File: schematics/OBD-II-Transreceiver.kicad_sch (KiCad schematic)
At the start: 5 parts, among them IC2 MCP2551T-E_SN, Q1 MOSFET, Q2 TRNSSTR

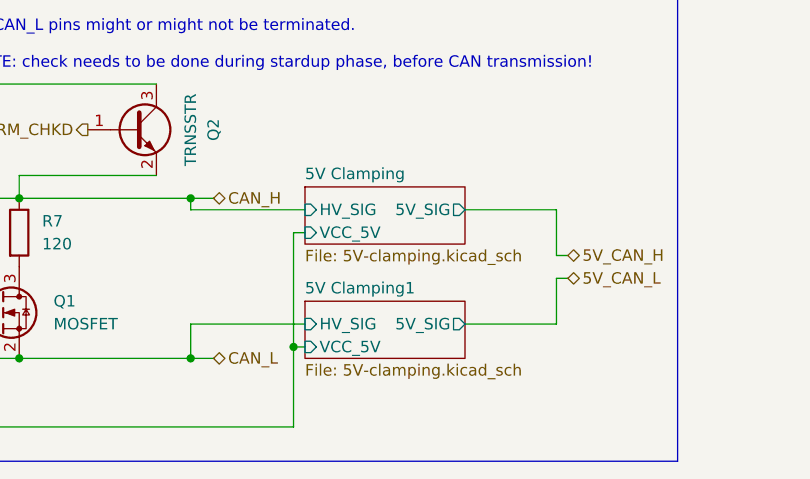
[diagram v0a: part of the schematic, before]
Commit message: OBD II clamping schematic simplification; README file update. Small repositionings.
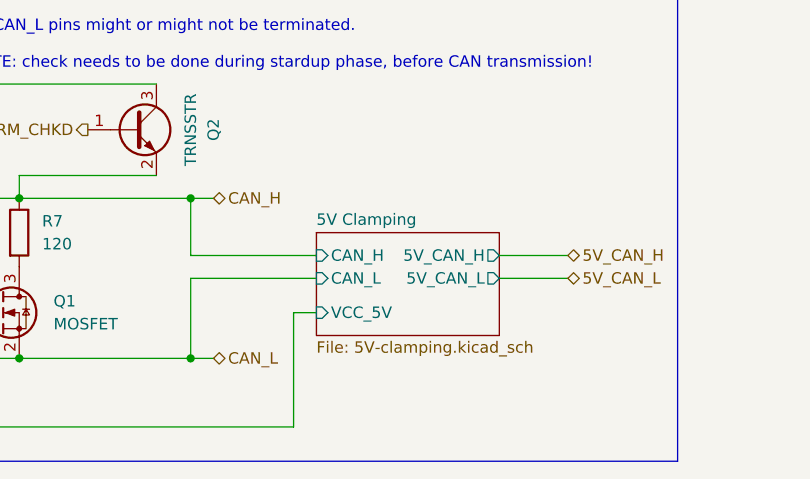
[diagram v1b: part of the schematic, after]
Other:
- removed sheet 5V Clamping1
- sheet 5V Clamping ports: added 5V_CAN_H, 5V_CAN_L, CAN_H, CAN_L; removed 5V_SIG, HV_SIG
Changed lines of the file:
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@@
+	)
+	(junction
+		(at 52.07 74.93)
+		(diameter 0)
+		(color 0 0 0 0)
 	)
 	(junction
@@
 	)
 	(junction
-		(at 148.59 73.66)
-		(diameter 0)
-		(color 0 0 0 0)
-	)
-	(junction
-		(at 52.07 74.93)
+		(at 118.11 74.93)
 		(diameter 0)
 		(color 0 0 0 0)
@@
 	)
 	(junction
-		(at 118.11 74.93)
-		(diameter 0)
-		(color 0 0 0 0)
-	)
-	(junction
 		(at 118.11 57.15)
 		(diameter 0)
@@
 	(wire
 		(pts
-			(xy 177.8 71.12) (xy 167.64 71.12)
+			(xy 137.16 63.5) (xy 151.13 63.5)
 		)
 		(stroke
@@
 	(wire
 		(pts
+			(xy 137.16 74.93) (xy 137.16 66.04)
+		)
+		(stroke
+			(width 0)
+			(type default)
+		)
+	)
+	(wire
+		(pts
+			(xy 148.59 69.85) (xy 151.13 69.85)
+		)
+		(stroke
+			(width 0)
+			(type default)
+		)
+	)
+	(wire
+		(pts
 			(xy 91.44 72.39) (xy 88.9 72.39)
 		)
@@
 	(wire
 		(pts
+			(xy 137.16 57.15) (xy 137.16 63.5)
+		)
+		(stroke
+			(width 0)
+			(type default)
+		)
+	)
+	(wire
+		(pts
 			(xy 91.44 57.15) (xy 91.44 72.39)
 		)
@@
 	(wire
 		(pts
-			(xy 137.16 74.93) (xy 137.16 71.12)
-		)
-		(stroke
-			(width 0)
-			(type default)
-		)
-	)
-	(wire
-		(pts
-			(xy 148.59 73.66) (xy 148.59 60.96)
-		)
-		(stroke
-			(width 0)
-			(type default)
-		)
-	)
-	(wire
-		(pts
 			(xy 118.11 57.15) (xy 137.16 57.15)
 		)
@@
 	(wire
 		(pts
-			(xy 137.16 58.42) (xy 149.86 58.42)
-		)
-		(stroke
-			(width 0)
-			(type default)
-		)
-	)
-	(wire
-		(pts
-			(xy 148.59 73.66) (xy 149.86 73.66)
-		)
-		(stroke
-			(width 0)
-			(type default)
-		)
-	)
-	(wire
-		(pts
-			(xy 137.16 57.15) (xy 137.16 58.42)
-		)
-		(stroke
-			(width 0)
-			(type default)
-		)
-	)
-	(wire
-		(pts
-			(xy 148.59 60.96) (xy 149.86 60.96)
+			(xy 52.07 54.61) (xy 52.07 74.93)
+		)
+		(stroke
+			(width 0)
+			(type default)
+		)
+	)
+	(wire
+		(pts
+			(xy 52.07 74.93) (xy 52.07 82.55)
+		)
+		(stroke
+			(width 0)
+			(type default)
+		)
+	)
+	(wire
+		(pts
+			(xy 118.11 74.93) (xy 137.16 74.93)
+		)
+		(stroke
+			(width 0)
+			(type default)
+		)
+	)
+	(wire
+		(pts
+			(xy 49.53 74.93) (xy 52.07 74.93)
+		)
+		(stroke
+			(width 0)
+			(type default)
+		)
+	)
+	(wire
+		(pts
+			(xy 133.35 54.61) (xy 118.11 54.61)
+		)
+		(stroke
+			(width 0)
+			(type default)
+		)
+	)
+	(wire
+		(pts
+			(xy 137.16 74.93) (xy 139.7 74.93)
+		)
+		(stroke
+			(width 0)
+			(type default)
+		)
+	)
+	(wire
+		(pts
+			(xy 101.6 54.61) (xy 52.07 54.61)
 		)
 		(stroke
@@
 	(wire
 		(pts
-			(xy 52.07 54.61) (xy 52.07 74.93)
-		)
-		(stroke
-			(width 0)
-			(type default)
-		)
-	)
-	(wire
-		(pts
-			(xy 177.8 63.5) (xy 179.07 63.5)
-		)
-		(stroke
-			(width 0)
-			(type default)
-		)
-	)
-	(wire
-		(pts
-			(xy 52.07 74.93) (xy 52.07 82.55)
-		)
-		(stroke
-			(width 0)
-			(type default)
-		)
-	)
-	(wire
-		(pts
-			(xy 177.8 66.04) (xy 177.8 71.12)
-		)
-		(stroke
-			(width 0)
-			(type default)
-		)
-	)
-	(wire
-		(pts
-			(xy 137.16 74.93) (xy 139.7 74.93)
-		)
-		(stroke
-			(width 0)
-			(type default)
-		)
-	)
-	(wire
-		(pts
-			(xy 49.53 74.93) (xy 52.07 74.93)
-		)
-		(stroke
-			(width 0)
-			(type default)
-		)
-	)
-	(wire
-		(pts
-			(xy 133.35 54.61) (xy 118.11 54.61)
-		)
-		(stroke
-			(width 0)
-			(type default)
-		)
-	)
-	(wire
-		(pts
-			(xy 101.6 54.61) (xy 52.07 54.61)
-		)
-		(stroke
-			(width 0)
-			(type default)
-		)
-	)
-	(wire
-		(pts
-			(xy 148.59 82.55) (xy 148.59 73.66)
+			(xy 171.45 63.5) (xy 179.07 63.5)
+		)
+		(stroke
+			(width 0)
+			(type default)
+		)
+	)
+	(wire
+		(pts
+			(xy 171.45 66.04) (xy 179.07 66.04)
 		)
 		(stroke
@@
 	(wire
 		(pts
-			(xy 137.16 71.12) (xy 149.86 71.12)
-		)
-		(stroke
-			(width 0)
-			(type default)
-		)
-	)
-	(wire
-		(pts
-			(xy 118.11 74.93) (xy 137.16 74.93)
-		)
-		(stroke
-			(width 0)
-			(type default)
-		)
-	)
-	(wire
-		(pts
-			(xy 177.8 66.04) (xy 179.07 66.04)
-		)
-		(stroke
-			(width 0)
-			(type default)
-		)
-	)
-	(wire
-		(pts
-			(xy 177.8 58.42) (xy 177.8 63.5)
+			(xy 148.59 82.55) (xy 148.59 69.85)
 		)
 		(stroke
@@
 	(wire
 		(pts
-			(xy 177.8 58.42) (xy 167.64 58.42)
+			(xy 137.16 66.04) (xy 151.13 66.04)
 		)
 		(stroke
@@
 	)
 	(sheet
-		(at 149.86 55.88)
-		(size 17.78 6.35)
+		(at 151.13 60.96)
+		(size 20.32 11.43)
 		(exclude_from_sim no)
 		(in_bom yes)
@@
 		)
 		(property "Sheetname" "5V Clamping"
-			(at 149.86 55.1684 0)
+			(at 151.13 60.2484 0)
 			(effects
 				(font
@@
 		)
 		(property "Sheetfile" "5V-clamping.kicad_sch"
-			(at 149.86 62.8146 0)
+			(at 151.13 72.9746 0)
 			(effects
 				(font
@@
 			)
 		)
-		(pin "5V_SIG" output
-			(at 167.64 58.42 0)
+		(pin "VCC_5V" input
+			(at 151.13 69.85 180)
+			(effects
+				(font
+					(size 1.27 1.27)
+				)
+				(justify left)
+			)
+		)
+		(pin "5V_CAN_H" output
+			(at 171.45 63.5 0)
 			(effects
 				(font
@@
 			)
 		)
-		(pin "HV_SIG" input
-			(at 149.86 58.42 180)
-			(effects
-				(font
-					(size 1.27 1.27)
-				)
-				(justify left)
-			)
-		)
-		(pin "VCC_5V" input
-			(at 149.86 60.96 180)
+		(pin "5V_CAN_L" output
+			(at 171.45 66.04 0)
+			(effects
+				(font
+					(size 1.27 1.27)
+				)
+				(justify right)
+			)
+		)
+		(pin "CAN_H" input
+			(at 151.13 63.5 180)
+			(effects
+				(font
+					(size 1.27 1.27)
+				)
+				(justify left)
+			)
+		)
+		(pin "CAN_L" input
+			(at 151.13 66.04 180)
 			(effects
 				(font
@@
 				)
 			)
-		)
-	)
-	(sheet
-		(at 149.86 68.58)
-		(size 17.78 6.35)
-		(exclude_from_sim no)
-		(in_bom yes)
-		(on_board yes)
-		(dnp no)
-		(fields_autoplaced yes)
-		(stroke
-			(width 0.1524)
-			(type solid)
-		)
-		(fill
-			(color 0 0 0 0.0000)
-		)
-		(property "Sheetname" "5V Clamping1"
-			(at 149.86 67.8684 0)
-			(effects
-				(font
-					(size 1.27 1.27)
-				)
-				(justify left bottom)
-			)
-		)
-		(property "Sheetfile" "5V-clamping.kicad_sch"
-			(at 149.86 75.5146 0)
-			(effects
-				(font
-					(size 1.27 1.27)
-				)
-				(justify left top)
-			)
-		)
-		(pin "5V_SIG" output
-			(at 167.64 71.12 0)
-			(effects
-				(font
-					(size 1.27 1.27)
-				)
-				(justify right)
-			)
-		)
-		(pin "HV_SIG" input
-			(at 149.86 71.12 180)
-			(effects
-				(font
-					(size 1.27 1.27)
-				)
-				(justify left)
-			)
-		)
-		(pin "VCC_5V" input
-			(at 149.86 73.66 180)
-			(effects
-				(font
-					(size 1.27 1.27)
-				)
-				(justify left)
-			)
-		)
-		(instances
-			(project "bike-sensors-logger"
-				(path "/2c1d9222-af16-428b-85a5-a3d420373d70/23f3389a-4f90-491e-9f31-2a46e142f2be"
-					(page "3")
-				)
-			)

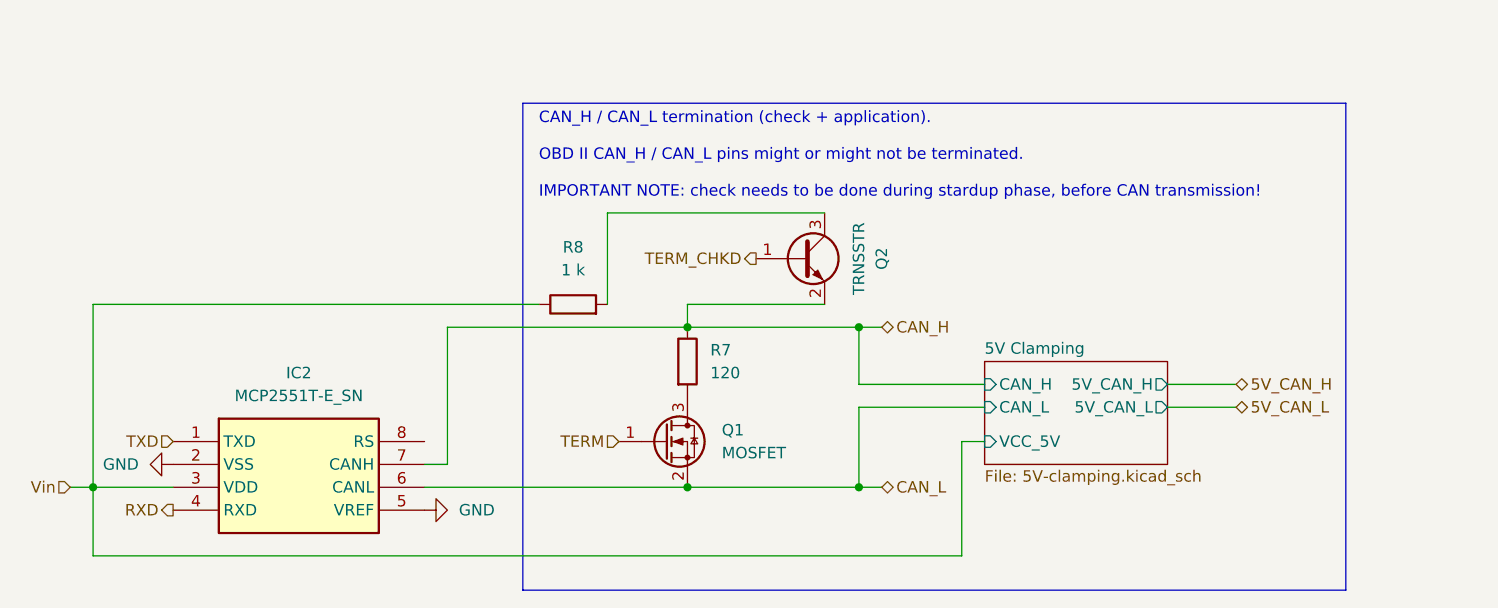
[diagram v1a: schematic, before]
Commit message: Fixed OBD II termination check (schem + firm)
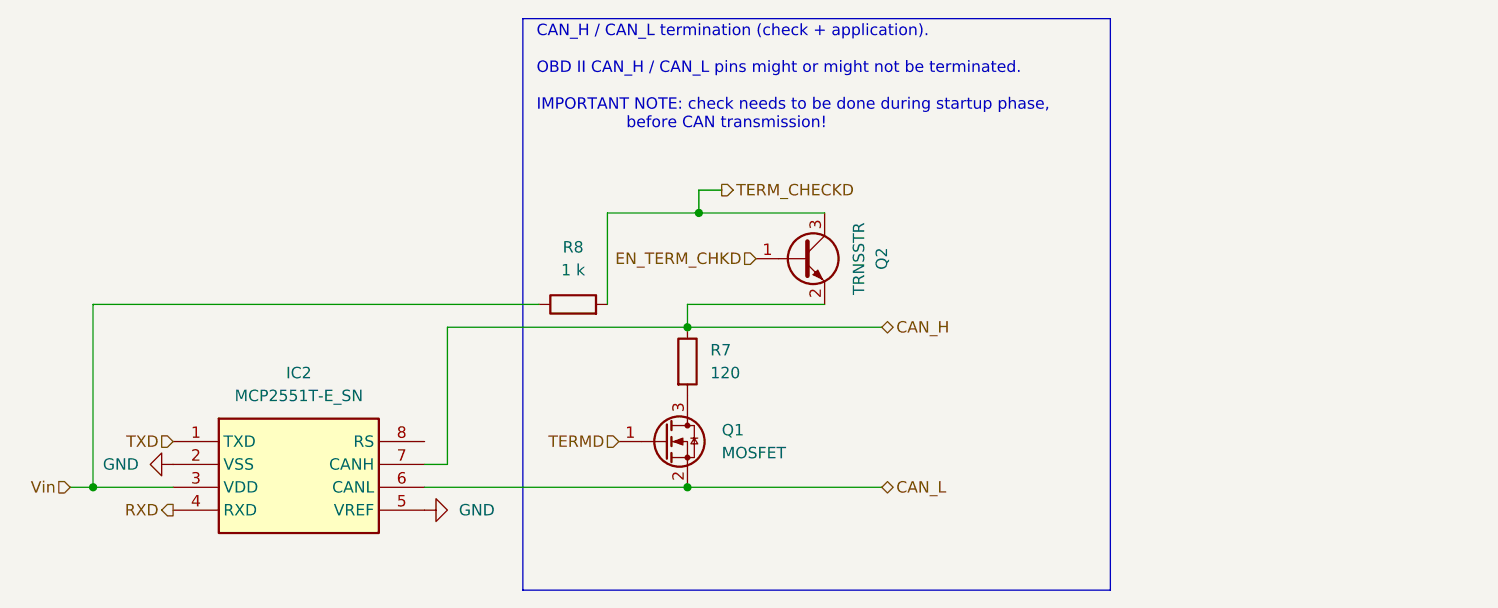
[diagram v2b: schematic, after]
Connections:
- net TERM_CHECKD: now reaches Q2.3 (C), R8.2
- net TERM renamed TERMD
- net TERM_CHKD renamed EN_TERM_CHKD
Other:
- removed sheet 5V Clamping
- note added: "CAN_H / CAN_L termination (check + application). OBD II CAN_H / CAN_L pins might or might not be terminated. IMPORTANT NOTE: check needs to be done during startup phase, before CAN transmission!"
- note removed: "CAN_H / CAN_L termination (check + application). OBD II CAN_H / CAN_L pins might or might not be terminated. IMPORTANT NOTE: check needs to be done during stardup phase, before CAN transmission!"
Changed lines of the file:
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@@
 	)
 	(rectangle
-		(start 99.822 32.258)
-		(end 191.262 86.36)
+		(start 99.822 22.86)
+		(end 165.1 86.36)
 		(stroke
 			(width 0)
@@
 		)
 	)
-	(text "CAN_H / CAN_L termination (check + application).\n\nOBD II CAN_H / CAN_L pins might or might not be terminated.\n\nIMPORTANT NOTE: check needs to be done during stardup phase, before CAN transmission!"
+	(text "CAN_H / CAN_L termination (check + application).\n\nOBD II CAN_H / CAN_L pins might or might not be terminated.\n\nIMPORTANT NOTE: check needs to be done during startup phase,\n                  before CAN transmission!"
 		(exclude_from_sim no)
-		(at 101.6 38.1 0)
+		(at 101.346 29.464 0)
 		(effects
 			(font
@@
 			(justify left)
 		)
+	)
+	(junction
+		(at 119.38 44.45)
+		(diameter 0)
+		(color 0 0 0 0)
 	)
 	(junction
@@
 	)
 	(junction
-		(at 137.16 74.93)
-		(diameter 0)
-		(color 0 0 0 0)
-	)
-	(junction
 		(at 118.11 74.93)
-		(diameter 0)
-		(color 0 0 0 0)
-	)
-	(junction
-		(at 137.16 57.15)
 		(diameter 0)
 		(color 0 0 0 0)
@@
 	(wire
 		(pts
-			(xy 137.16 63.5) (xy 151.13 63.5)
-		)
-		(stroke
-			(width 0)
-			(type default)
-		)
-	)
-	(wire
-		(pts
 			(xy 109.22 54.61) (xy 109.22 44.45)
 		)
@@
 	(wire
 		(pts
-			(xy 137.16 74.93) (xy 137.16 66.04)
-		)
-		(stroke
-			(width 0)
-			(type default)
-		)
-	)
-	(wire
-		(pts
-			(xy 148.59 69.85) (xy 151.13 69.85)
-		)
-		(stroke
-			(width 0)
-			(type default)
-		)
-	)
-	(wire
-		(pts
 			(xy 91.44 72.39) (xy 88.9 72.39)
 		)
@@
 	(wire
 		(pts
-			(xy 109.22 44.45) (xy 133.35 44.45)
-		)
-		(stroke
-			(width 0)
-			(type default)
-		)
-	)
-	(wire
-		(pts
 			(xy 91.44 57.15) (xy 118.11 57.15)
 		)
@@
 	(wire
 		(pts
-			(xy 137.16 57.15) (xy 137.16 63.5)
-		)
-		(stroke
-			(width 0)
-			(type default)
-		)
-	)
-	(wire
-		(pts
 			(xy 91.44 57.15) (xy 91.44 72.39)
 		)
@@
 	(wire
 		(pts
-			(xy 118.11 57.15) (xy 137.16 57.15)
+			(xy 118.11 57.15) (xy 139.7 57.15)
 		)
 		(stroke
@@
 	(wire
 		(pts
-			(xy 52.07 74.93) (xy 52.07 82.55)
-		)
-		(stroke
-			(width 0)
-			(type default)
-		)
-	)
-	(wire
-		(pts
-			(xy 118.11 74.93) (xy 137.16 74.93)
+			(xy 119.38 41.91) (xy 119.38 44.45)
+		)
+		(stroke
+			(width 0)
+			(type default)
+		)
+	)
+	(wire
+		(pts
+			(xy 109.22 44.45) (xy 119.38 44.45)
+		)
+		(stroke
+			(width 0)
+			(type default)
+		)
+	)
+	(wire
+		(pts
+			(xy 119.38 44.45) (xy 133.35 44.45)
+		)
+		(stroke
+			(width 0)
+			(type default)
+		)
+	)
+	(wire
+		(pts
+			(xy 118.11 74.93) (xy 139.7 74.93)
 		)
 		(stroke
@@
 	(wire
 		(pts
-			(xy 137.16 74.93) (xy 139.7 74.93)
-		)
-		(stroke
-			(width 0)
-			(type default)
-		)
-	)
-	(wire
-		(pts
 			(xy 101.6 54.61) (xy 52.07 54.61)
 		)
@@
 	(wire
 		(pts
-			(xy 137.16 57.15) (xy 139.7 57.15)
-		)
-		(stroke
-			(width 0)
-			(type default)
-		)
-	)
-	(wire
-		(pts
-			(xy 171.45 63.5) (xy 179.07 63.5)
-		)
-		(stroke
-			(width 0)
-			(type default)
-		)
-	)
-	(wire
-		(pts
-			(xy 171.45 66.04) (xy 179.07 66.04)
+			(xy 121.92 41.91) (xy 119.38 41.91)
 		)
 		(stroke
@@
 		(pts
 			(xy 52.07 74.93) (xy 60.96 74.93)
-		)
-		(stroke
-			(width 0)
-			(type default)
-		)
-	)
-	(wire
-		(pts
-			(xy 148.59 82.55) (xy 148.59 69.85)
-		)
-		(stroke
-			(width 0)
-			(type default)
-		)
-	)
-	(wire
-		(pts
-			(xy 52.07 82.55) (xy 148.59 82.55)
-		)
-		(stroke
-			(width 0)
-			(type default)
-		)
-	)
-	(wire
-		(pts
-			(xy 137.16 66.04) (xy 151.13 66.04)
 		)
 		(stroke
@@
 		)
 	)
-	(hierarchical_label "5V_CAN_L"
-		(shape bidirectional)
-		(at 179.07 66.04 0)
-		(effects
-			(font
-				(size 1.27 1.27)
-			)
-			(justify left)
-		)
-	)
 	(hierarchical_label "TXD"
 		(shape input)
@@
 		)
 	)
-	(hierarchical_label "TERM"
+	(hierarchical_label "TERMD"
 		(shape input)
 		(at 110.49 69.85 180)
@@
 		)
 	)
-	(hierarchical_label "5V_CAN_H"
-		(shape bidirectional)
-		(at 179.07 63.5 0)
-		(effects
-			(font
-				(size 1.27 1.27)
-			)
-			(justify left)
-		)
-	)
-	(hierarchical_label "TERM_CHKD"
-		(shape output)
+	(hierarchical_label "EN_TERM_CHKD"
+		(shape input)
 		(at 125.73 49.53 180)
 		(effects
@@
 		(shape bidirectional)
 		(at 139.7 74.93 0)
+		(effects
+			(font
+				(size 1.27 1.27)
+			)
+			(justify left)
+		)
+	)
+	(hierarchical_label "TERM_CHECKD"
+		(shape output)
+		(at 121.92 41.91 0)
 		(effects
 			(font
@@
 				)
 			)
-		)
-	)
-	(sheet
-		(at 151.13 60.96)
-		(size 20.32 11.43)
-		(exclude_from_sim no)
-		(in_bom yes)
-		(on_board yes)
-		(dnp no)
-		(fields_autoplaced yes)
-		(stroke
-			(width 0.1524)
-			(type solid)
-		)
-		(fill
-			(color 0 0 0 0.0000)
-		)
-		(property "Sheetname" "5V Clamping"
-			(at 151.13 60.2484 0)
-			(effects
-				(font
-					(size 1.27 1.27)
-				)
-				(justify left bottom)
-			)
-		)
-		(property "Sheetfile" "5V-clamping.kicad_sch"
-			(at 151.13 72.9746 0)
-			(effects
-				(font
-					(size 1.27 1.27)
-				)
-				(justify left top)
-			)
-		)
-		(pin "VCC_5V" input
-			(at 151.13 69.85 180)
-			(effects
-				(font
-					(size 1.27 1.27)
-				)
-				(justify left)
-			)
-		)
-		(pin "5V_CAN_H" output
-			(at 171.45 63.5 0)
-			(effects
-				(font
-					(size 1.27 1.27)
-				)
-				(justify right)
-			)
-		)
-		(pin "5V_CAN_L" output
-			(at 171.45 66.04 0)
-			(effects
-				(font
-					(size 1.27 1.27)
-				)
-				(justify right)
-			)
-		)
-		(pin "CAN_H" input
-			(at 151.13 63.5 180)
-			(effects
-				(font
-					(size 1.27 1.27)
-				)
-				(justify left)
-			)
-		)
-		(pin "CAN_L" input
-			(at 151.13 66.04 180)
-			(effects
-				(font
-					(size 1.27 1.27)
-				)
-				(justify left)
-			)
-		)
-		(instances
-			(project "bike-sensors-logger"
-				(path "/2c1d9222-af16-428b-85a5-a3d420373d70/23f3389a-4f90-491e-9f31-2a46e142f2be"
-					(page "6")
-				)
-			)

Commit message: Micro SD
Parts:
- R7, R8: footprint (none) -> Resistor_SMD:R_0603_1608Metric
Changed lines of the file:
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@@
 			)
 		)
-		(property "Footprint" ""
+		(property "Footprint" "Resistor_SMD:R_0603_1608Metric"
 			(at 105.41 56.388 90)
 			(effects
@@
 			)
 		)
-		(property "Footprint" ""
+		(property "Footprint" "Resistor_SMD:R_0603_1608Metric"
 			(at 116.332 60.96 90)
 			(effects

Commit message: Integrated 3V3 buck converter due to Arduino's current limits
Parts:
- IC2: footprint SOIC127P600X175-8N -> MCP2551-E-SN:SOIC127P600X175-8N
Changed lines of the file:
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@@
 			)
 		)
-		(property "Footprint" "SOIC127P600X175-8N"
+		(property "Footprint" "MCP2551-E-SN:SOIC127P600X175-8N"
 			(at 85.09 164.77 0)
 			(effects
